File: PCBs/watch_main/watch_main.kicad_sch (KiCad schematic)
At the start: 0 parts

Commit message: More PCB progress
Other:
- sheet Display Connector ports: added DSI_TE, PCD, RESET; removed none
- sheet FPGA ports: added CDONE, CRESET_B, INT; removed none
- sheet Flash ports: added CS2, INT, RST; removed none
- sheet GNSS ports: added PPS, PRG, RST, WAKEUP; removed none
- sheet Micro SD ports: added CD; removed SD_CD, SD_EN
- sheet Power ports: added INT; removed none
- sheet RFID ports: added CARRIER, OUT, PULL, RF_IN, SHDN; removed none
- sheet STM32 ports: added CRS_SYNC, DISPLAY_PCD, DISPLAY_RST, DSI_TE, FLASH_CS2, FLASH_INT, FLASH_RST, FPGA_CDONE, FPGA_CRESET_B, FPGA_INT, GNSS_PRG, GNSS_RST, GNSS_WAKEUP, PWR_INT, RFID_CARRIER, RFID_OUT, RFID_PULL, RFID_RF_IN, RFID_SHDN; removed SD_EN
- note added: "Circuits & ICs"
- note added: "Interfaces"
- note added: "Microcontrollers"
- note added: "Oscillators"

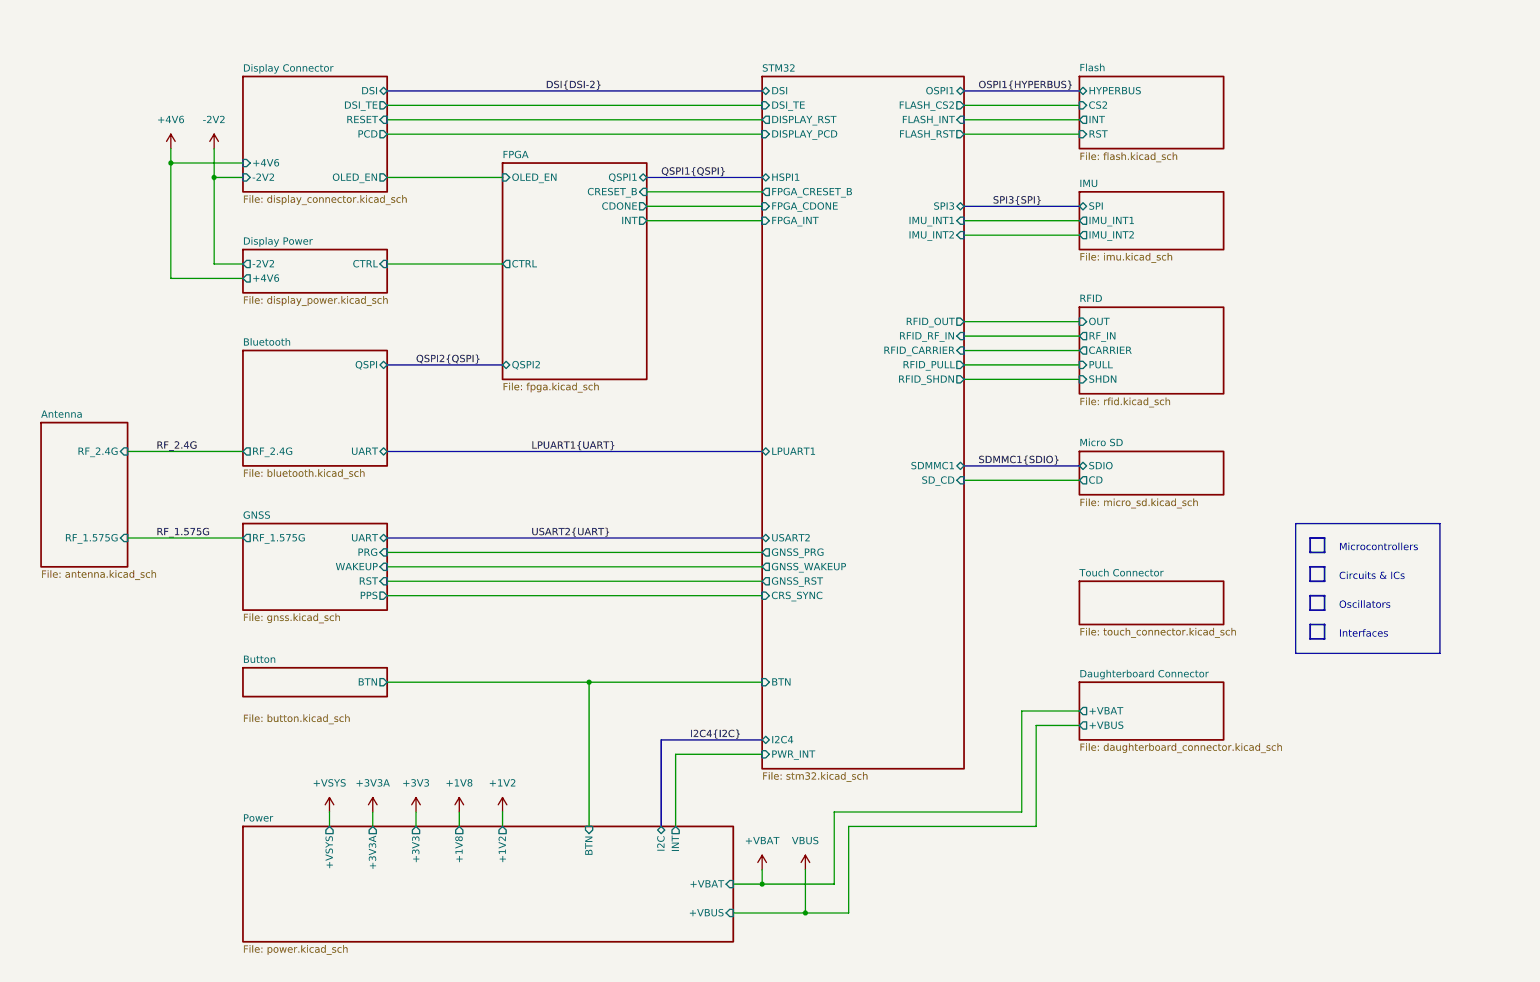
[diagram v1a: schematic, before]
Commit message: Created "Component Selection.md", minor PCB schematic updates
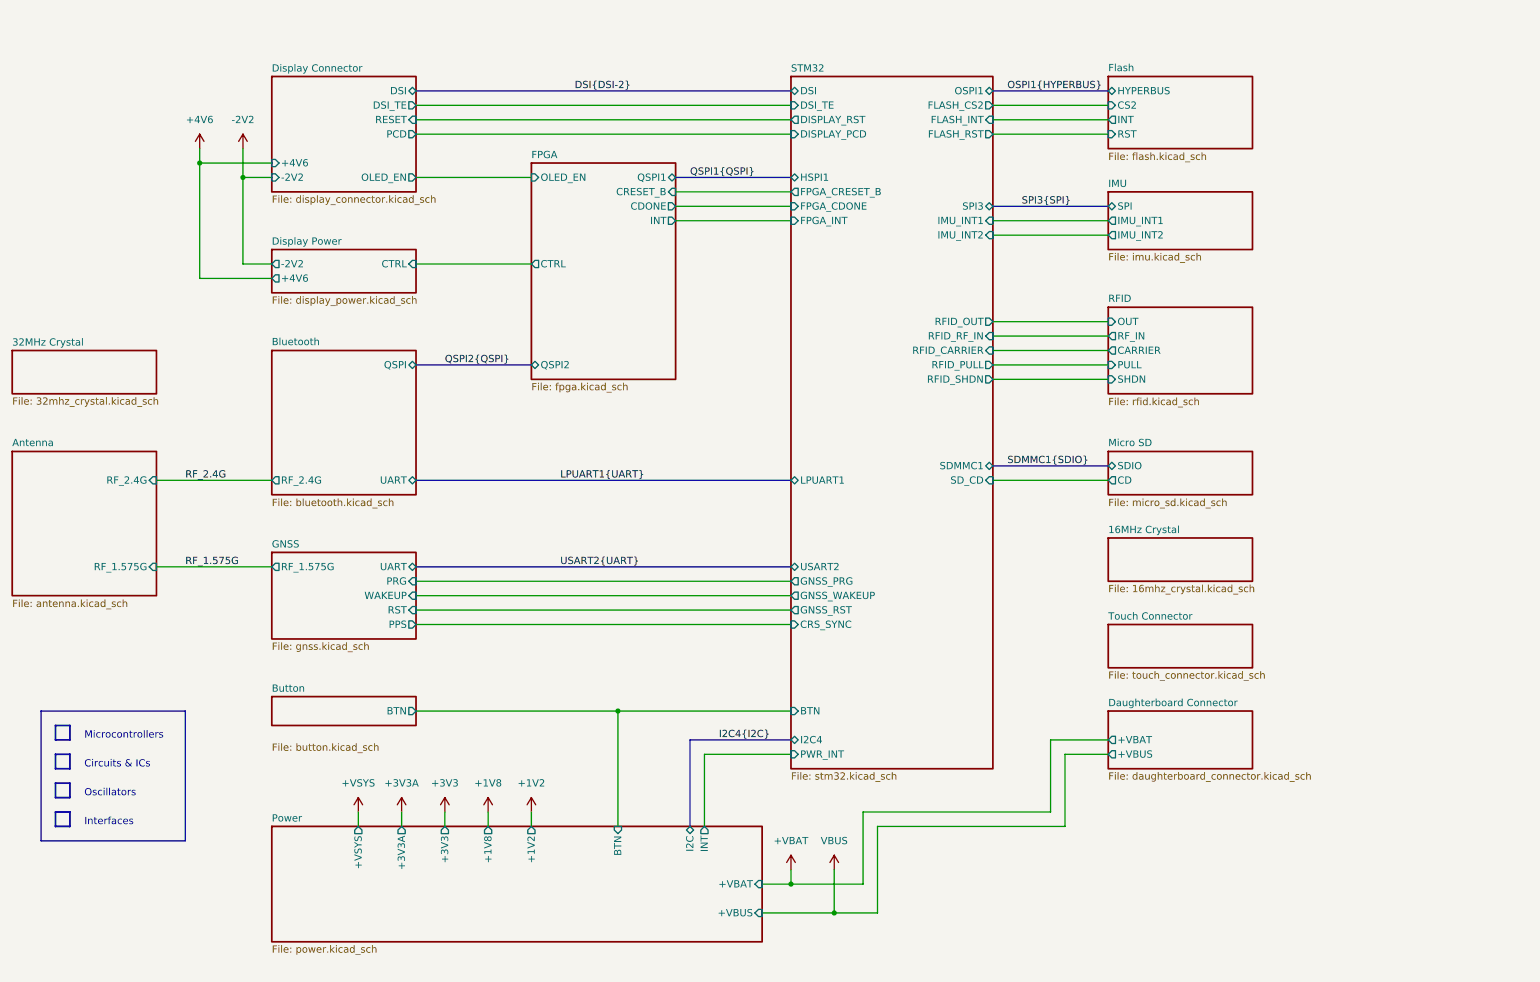
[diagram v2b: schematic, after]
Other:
- added sheet 16MHz Crystal (16mhz_crystal.kicad_sch)
- added sheet 32MHz Crystal (32mhz_crystal.kicad_sch)

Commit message: Created firmware project
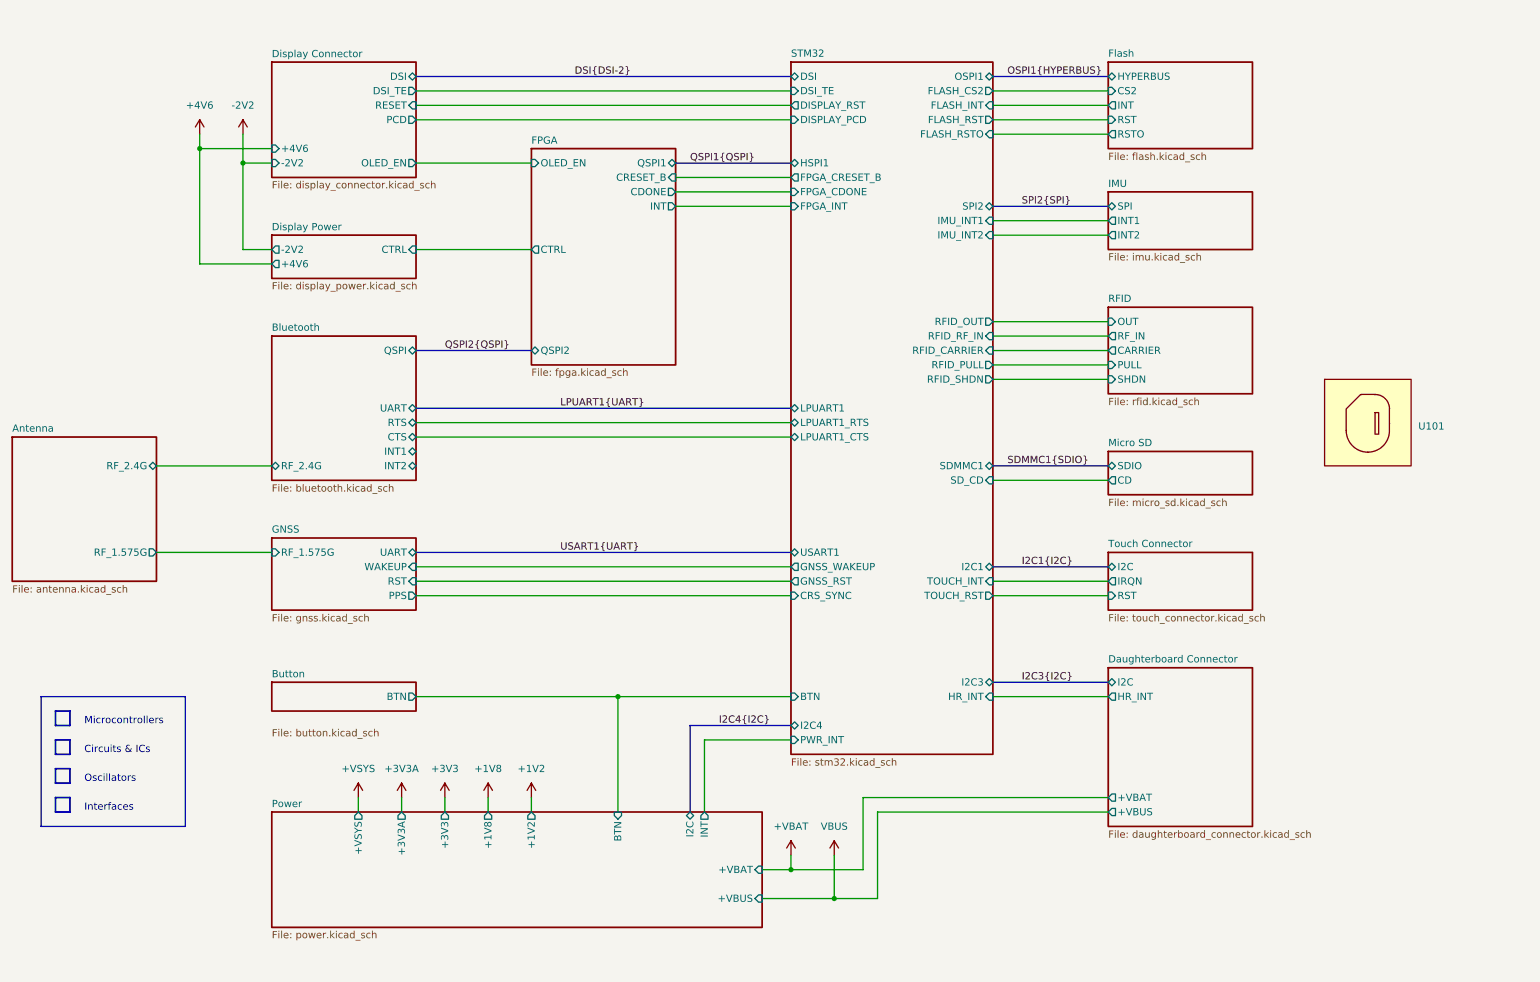
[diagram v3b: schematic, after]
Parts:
- added U101: ~, watch_footprints:Watch Outline V1, symbol watch_symbols_lib:Outline
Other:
- removed sheet 16MHz Crystal
- removed sheet 32MHz Crystal
- sheet Bluetooth ports: added CTS, INT1, INT2, RTS; removed none
- sheet Daughterboard Connector ports: added HR_INT, I2C; removed none
- sheet Flash ports: added RSTO; removed none
- sheet GNSS ports: added none; removed PRG
- sheet IMU ports: added INT1, INT2; removed IMU_INT1, IMU_INT2
- sheet STM32 ports: added FLASH_RSTO, HR_INT, I2C1, I2C3, LPUART1_CTS, LPUART1_RTS, SPI2, TOUCH_INT, TOUCH_RST, USART1; removed GNSS_PRG, SPI3, USART2
- sheet Touch Connector ports: added I2C, IRQN, RST; removed none

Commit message: Schematic and pcb progress
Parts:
- removed U101: ~, watch_footprints:Watch Outline V1, symbol watch_symbols_lib:Outline
- added U101: Watch_Outline, watch_footprints:Watch Outline V1, symbol watch_symbols_lib:Watch_Outline
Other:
- sheet STM32 ports: added BT_INT1, BT_INT2; removed none
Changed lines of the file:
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@@
+    (stroke (width 0) (type default))
+  )
+  (wire (pts (xy 91.44 96.52) (xy 157.48 96.52))
+    (stroke (width 0) (type default))
+  )
+  (wire (pts (xy 91.44 93.98) (xy 157.48 93.98))
     (stroke (width 0) (type default))
   )
@@
     )
   )
+  (symbol (lib_id "watch_symbols_lib:Watch_Outline") (at 261.62 83.82 0) (unit 1)
+    (in_bom no) (on_board yes) (dnp no) (fields_autoplaced)
+    (property "Reference" "U101" (at 270.51 83.185 0)
+      (effects (font (size 1.27 1.27)) (justify left))
+    )
+    (property "Value" "Watch_Outline" (at 270.51 85.725 0)
+      (effects (font (size 1.27 1.27)) (justify left))
+    )
+    (property "Footprint" "watch_footprints:Watch Outline V1" (at 261.62 93.98 0)
+      (effects (font (size 1.27 1.27)) hide)
+    )
+    (property "Datasheet" "" (at 260.35 79.375 0)
+      (effects (font (size 1.27 1.27)) hide)
+    )
+    (property "Sim.Enable" "0" (at 262.89 95.885 0)
+      (effects (font (size 1.27 1.27)) hide)
+    )
+    (instances
+      (project "watch_main"
+        (path "/b008648a-c7cf-4e14-8a0a-b9314d757b4a"
+          (reference "U101") (unit 1)
+        )
+      )
+    )
+  )
   (symbol (lib_id "watch_symbols_lib:+3V3A") (at 88.9 154.94 0) (unit 1)
     (in_bom yes) (on_board yes) (dnp no) (fields_autoplaced)
@@
         (path "/b008648a-c7cf-4e14-8a0a-b9314d757b4a"
           (reference "#PWR0102") (unit 1)
-        )
-      )
-    )
-  )
-  (symbol (lib_id "watch_symbols_lib:Outline") (at 259.08 88.9 0) (unit 1)
-    (in_bom no) (on_board yes) (dnp no) (fields_autoplaced)
-    (property "Reference" "U101" (at 267.97 89.535 0)
-      (effects (font (size 1.27 1.27)) (justify left))
-    )
-    (property "Value" "~" (at 257.81 84.455 0)
-      (effects (font (size 1.27 1.27)))
-    )
-    (property "Footprint" "watch_footprints:Watch Outline V1" (at 259.08 99.06 0)
-      (effects (font (size 1.27 1.27)) hide)
-    )
-    (property "Datasheet" "" (at 257.81 84.455 0)
-      (effects (font (size 1.27 1.27)) hide)
-    )
-    (property "Sim.Enable" "0" (at 260.35 100.965 0)
-      (effects (font (size 1.27 1.27)) hide)
-    )
-    (instances
-      (project "watch_main"
-        (path "/b008648a-c7cf-4e14-8a0a-b9314d757b4a"
-          (reference "U101") (unit 1)
         )
       )
@@
       (effects (font (size 1.27 1.27)) (justify right))
     )
-    (instances
+    (pin "BT_INT1" bidirectional (at 157.48 93.98 180)
+      (effects (font (size 1.27 1.27)) (justify left))
+    )
+    (pin "BT_INT2" bidirectional (at 157.48 96.52 180)
+      (effects (font (size 1.27 1.27)) (justify left))
+    )
+    (instances

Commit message: PCB Schematic progress
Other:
- sheet Bluetooth ports: added INT3; removed none
- sheet FPGA ports: added INT_NRF, INT_STM; removed INT
- moved on the sheet: U101

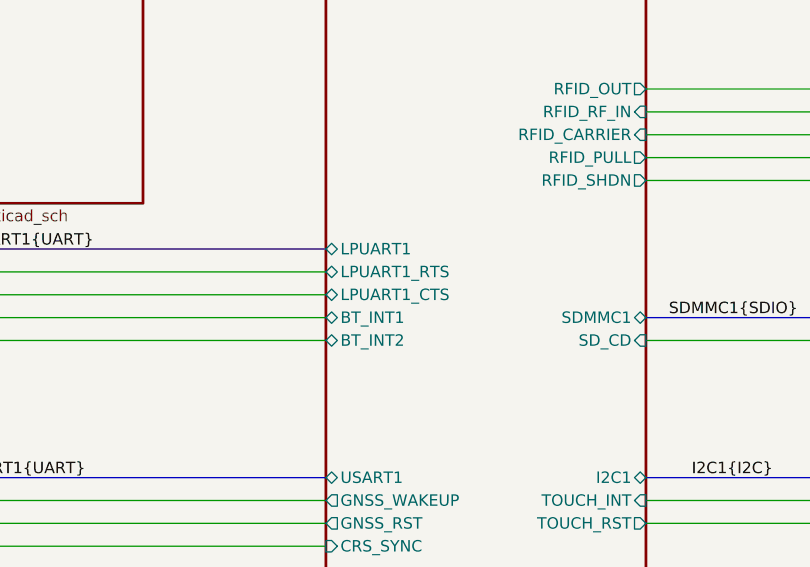
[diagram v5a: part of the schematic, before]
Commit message: Added connector symbols and footprints
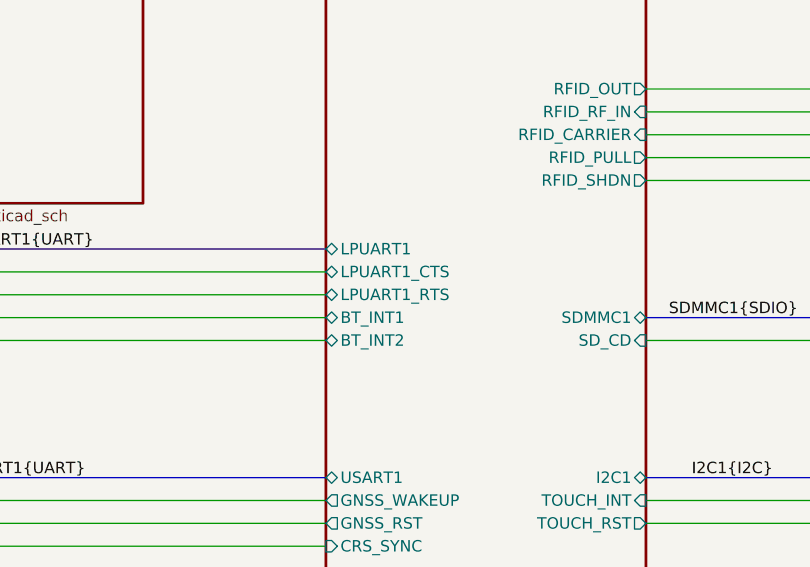
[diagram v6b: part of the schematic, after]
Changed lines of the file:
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@@
+    (stroke (width 0) (type default))
+  )
+  (wire (pts (xy 91.44 93.98) (xy 157.48 93.98))
     (stroke (width 0) (type default))
   )
@@
     (stroke (width 0) (type default))
   )
+  (wire (pts (xy 91.44 91.44) (xy 157.48 91.44))
+    (stroke (width 0) (type default))
+  )
   (wire (pts (xy 91.44 119.38) (xy 157.48 119.38))
     (stroke (width 0) (type default))
@@
     (stroke (width 0) (type default))
   )
-  (wire (pts (xy 91.44 93.98) (xy 157.48 93.98))
-    (stroke (width 0) (type default))
-  )
   (wire (pts (xy 193.04 119.38) (xy 213.36 119.38))
     (stroke (width 0) (type default))
@@
   )
   (wire (pts (xy 193.04 71.12) (xy 213.36 71.12))
-    (stroke (width 0) (type default))
-  )
-  (wire (pts (xy 91.44 91.44) (xy 157.48 91.44))
     (stroke (width 0) (type default))
   )
@@
       (effects (font (size 1.27 1.27)) (justify right))
     )
-    (pin "LPUART1_RTS" bidirectional (at 157.48 91.44 180)
-      (effects (font (size 1.27 1.27)) (justify left))
-    )
-    (pin "LPUART1_CTS" bidirectional (at 157.48 93.98 180)
-      (effects (font (size 1.27 1.27)) (justify left))
-    )
+    (pin "LPUART1_RTS" bidirectional (at 157.48 93.98 180)
+      (effects (font (size 1.27 1.27)) (justify left))
+    )
+    (pin "LPUART1_CTS" bidirectional (at 157.48 91.44 180)
+      (effects (font (size 1.27 1.27)) (justify left))
+    )

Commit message: Main PCB schematic almost complete
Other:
- removed sheet IMU
- added sheet Sensors (sensors.kicad_sch)
- sheet STM32 ports: added ALS_INT, MAG_INT; removed SPI2
- moved on the sheet: U101
